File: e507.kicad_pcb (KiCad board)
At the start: 2 copper layers, 1 part

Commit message: work on pcb
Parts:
- added C1: 1µF, Package_DFN_QFN:VQFN-16-1EP_3x3mm_P0.5mm_EP1.6x1.6mm, F.Cu at (178.6, 88.5)
- added C2: 10µF, Package_DFN_QFN:VQFN-16-1EP_3x3mm_P0.5mm_EP1.6x1.6mm, F.Cu at (178.6, 93.8)
- added C3: 1µF, Package_DFN_QFN:VQFN-16-1EP_3x3mm_P0.5mm_EP1.6x1.6mm, F.Cu at (178.6, 99.1)
- added C4: 22µF, Package_DFN_QFN:VQFN-16-1EP_3x3mm_P0.5mm_EP1.6x1.6mm, F.Cu at (178.6, 104.4)
- added C5: 47µF, Package_DFN_QFN:VQFN-16-1EP_3x3mm_P0.5mm_EP1.6x1.6mm, F.Cu at (178.6, 109.8)
- added D1: SMAJ5.0A, Diode_SMD:D_SMA, F.Cu at (187.5, 147.0)
- added J1: GT-USB-7010ASV, usb-port:AMPHENOL_12402012E212A, F.Cu at (196.5, 150.9)
- added J2: DM3CS-SF, microsd:HRS_DM3CS-SF, F.Cu at (192.5, 128.0)
- added J3: SJ-3523-SMT-TR, audio-jack:CUI_SJ-3523-SMT-TR, F.Cu at (197.0, 78.0)
- added J4: SCREEN, Connector:FanPinHeader_1x04_P2.54mm_Vertical, F.Cu at (203.8, 122.7)
- added P1: S2B-PH-SM4-TB, battery-connector:JST_S2B-PH-SM4-TB, F.Cu at (201.2, 139.7)
- added S2: BOOT, flat-button:SW_TS-1088-AR02016, F.Cu at (197.1, 116.5)
- added S3: VOLUME UP, side-button:SW_TL3340AF160QG, F.Cu at (187.0, 74.0)
- added S4: VOLUME DOWN, side-button:SW_TL3340AF160QG, F.Cu at (206.2, 74.0)
- added U1: BQ25185DLHR, charger:IC_BQ25185DLHR, F.Cu at (205.1, 148.7)
- added U2: TPS73633DBVT, ldo:SOT95P280X145-5N, F.Cu at (188.3, 86.5)
- added U3: TPS631000DRLR, buck-boost:SOT50P160X60-8N, F.Cu at (204.3, 132.2)
- added U4: ESP32-S3-WROOM-1U-N16R8, esp32:XCVR_ESP32-S3-WROOM-1U-N16R8, F.Cu at (196.8, 100.6)
- added U5: HS HS91L02W2C01, Display:ER_OLEDM0.91_1x-I2C, F.Cu at (220.2, 93.5)
- added U6: PCM5102APWR, dac:SOP65P640X120-20N, F.Cu at (204.5, 86.0)
- added U7: TPA6132A2RTER, amp:QFN50P300X300X80-16N, F.Cu at (197.0, 88.3)
- added U8: USBLC6-2SC6, Package_TO_SOT_SMD:SOT-23-6, F.Cu at (196.5, 142.5)
- S1: value TS-1088-AR02016 -> RESET
- moved S1 107.8 mm to (189.9, 116.5)
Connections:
- S1 pad 1: unconnected-(S1-Pad1) -> /MCU/IO_EN
- S1 pad 2: unconnected-(S1-Pad2) -> GND

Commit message: fucker
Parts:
- added U5: ER_OLEDM0.91_1x-I2C, Display:ER_OLEDM0.91_1x-I2C, F.Cu at (239.0, 87.3)
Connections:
- J1 pad A6: Net-(J1-D+_A) -> /MCU/USB_D+
- J1 pad A7: Net-(J1-D-_A) -> /MCU/USB_D-
- J1 pad B6: Net-(J1-D+_A) -> /MCU/USB_D+
- J1 pad B7: Net-(J1-D-_A) -> /MCU/USB_D-
- J3 pad 1: unconnected-(J3-SLEEVE-Pad1) -> GNDA
- J3 pad 2: unconnected-(J3-TIP-Pad2) -> Net-(J3-TIP)
- J3 pad 3: unconnected-(J3-RING-Pad3) -> Net-(J3-RING)
- U1 pad 3: /MCU/IO_CHG_STAT2 -> /MCU/IO_CHG_STAT1
- U1 pad 9: /MCU/IO_CHG_STAT1 -> /MCU/IO_CHG_STAT2
- U2 pad 3: /MCU/IO_AUDIO_EN -> /Audio/IO_AMP_EN
- U4 pad 10: /Audio/IO_DAC_BCK -> unconnected-(U4-IO17-Pad10)
- U4 pad 11: /Audio/IO_DAC_LRCK -> unconnected-(U4-IO18-Pad11)
- U4 pad 23: unconnected-(U4-IO21-Pad23) -> /Audio/IO_DAC_SCK
- U4 pad 28: unconnected-(U4-IO35-Pad28) -> /Audio/IO_DAC_DIN
- U4 pad 29: unconnected-(U4-IO36-Pad29) -> /Audio/IO_DAC_BCK
- U4 pad 30: unconnected-(U4-IO37-Pad30) -> /Audio/IO_DAC_LRCK
- U4 pad 8: /MCU/IO_AUDIO_EN -> /Audio/IO_AMP_EN
- U4 pad 9: /Audio/IO_DAC_DIN -> unconnected-(U4-IO16-Pad9)
- U6 pad 12: GND -> /Audio/IO_DAC_SCK
- U6 pad 3: GND -> GNDA
- U6 pad 6: unconnected-(U6-OUTL-Pad6) -> Net-(U6-OUTL)
- U6 pad 7: unconnected-(U6-OUTR-Pad7) -> Net-(U6-OUTR)
- U6 pad 9: GND -> GNDA
- U7 pad 1: unconnected-(U7-INL--Pad1) -> Net-(U7-INL-)
- U7 pad 10: unconnected-(U7-PGND-Pad10) -> GND
- U7 pad 11: unconnected-(U7-CPP-Pad11) -> Net-(U7-CPP)
- U7 pad 12: unconnected-(U7-HPVDD-Pad12) -> Net-(U7-HPVDD)
- U7 pad 13: unconnected-(U7-EN-Pad13) -> /Audio/IO_AMP_EN
- U7 pad 14: unconnected-(U7-VDD-Pad14) -> VSYS
- U7 pad 15: unconnected-(U7-SGND-Pad15) -> GNDA
- U7 pad 16: unconnected-(U7-OUTL-Pad16) -> Net-(J3-TIP)
- U7 pad 17: unconnected-(U7-EP-Pad17) -> GND
- U7 pad 2: unconnected-(U7-INL+-Pad2) -> GND
- U7 pad 3: unconnected-(U7-INR+-Pad3) -> GND
- U7 pad 4: unconnected-(U7-INR--Pad4) -> Net-(U7-INR-)
- U7 pad 5: unconnected-(U7-OUTR-Pad5) -> Net-(J3-RING)
- U7 pad 8: unconnected-(U7-HPVSS-Pad8) -> Net-(U7-HPVSS)
- U7 pad 9: unconnected-(U7-CPN-Pad9) -> Net-(U7-CPN)

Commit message: Finish? schematic
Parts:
- removed the U5 at (239.0, 87.3)
- removed the U5 at (220.2, 93.5)
- removed U8: USBLC6-2SC6, Package_TO_SOT_SMD:SOT-23-6
- added U5: USBLC6-2SC6, Package_TO_SOT_SMD:SOT-23-6, F.Cu at (195.9, 142.9)
- moved J4 11.4 mm to (192.5, 121.5)
- moved J2 5.10 mm to (191.5, 133.0)
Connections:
- D1 pad 1: GND -> VBUS
- D1 pad 2: VBUS -> GND
- J1 pad A6: /MCU/USB_D+ -> Net-(J1-D+_A)
- J1 pad A7: /MCU/USB_D- -> Net-(J1-D-_A)
- J1 pad B6: /MCU/USB_D+ -> Net-(J1-D+_A)
- J1 pad B7: /MCU/USB_D- -> Net-(J1-D-_A)
- U2 pad 2: GND -> GNDA
- U4 pad 10: unconnected-(U4-IO17-Pad10) -> /Audio/IO_DAC_BCK
- U4 pad 11: unconnected-(U4-IO18-Pad11) -> /Audio/IO_DAC_LRCK
- U4 pad 23: /Audio/IO_DAC_SCK -> unconnected-(U4-IO21-Pad23)
- U4 pad 28: /Audio/IO_DAC_DIN -> unconnected-(U4-IO35-Pad28)
- U4 pad 29: /Audio/IO_DAC_BCK -> unconnected-(U4-IO36-Pad29)
- U4 pad 30: /Audio/IO_DAC_LRCK -> unconnected-(U4-IO37-Pad30)
- U4 pad 9: unconnected-(U4-IO16-Pad9) -> /Audio/IO_DAC_DIN
- U6 pad 12: /Audio/IO_DAC_SCK -> GND
- U7 pad 6: unconnected-(U7-G0-Pad6) -> VSYS
- U7 pad 7: unconnected-(U7-G1-Pad7) -> GND

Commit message: holy routing
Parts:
- added C10: 1uF, Capacitor_SMD:C_0201_0603Metric, F.Cu at (71.1, 84.2)
- added C11: 1uF, Capacitor_SMD:C_0201_0603Metric, F.Cu at (71.2, 92.8)
- added C12: 0.1μF, Capacitor_SMD:C_0201_0603Metric, F.Cu at (24.5, 18.5)
- added C13: 10μF, Capacitor_SMD:C_0201_0603Metric, F.Cu at (24.5, 20.2)
- added C14: 2.2μF, Capacitor_SMD:C_0201_0603Metric, F.Cu at (24.5, 22.0)
- added C15: 2.2μF, Capacitor_SMD:C_0201_0603Metric, F.Cu at (24.5, 23.8)
- added C16: 0.1μF, Capacitor_SMD:C_0201_0603Metric, F.Cu at (24.5, 25.5)
- added C17: 10μF, Capacitor_SMD:C_0201_0603Metric, F.Cu at (24.5, 27.2)
- added C18: 0.1μF, Capacitor_SMD:C_0201_0603Metric, F.Cu at (24.5, 29.0)
- added C19: 10μF, Capacitor_SMD:C_0201_0603Metric, F.Cu at (26.9, 18.5)
- added C20: 10μF, Capacitor_SMD:C_0201_0603Metric, F.Cu at (26.9, 20.2)
- added C21: 0.1μF, Capacitor_SMD:C_0201_0603Metric, F.Cu at (26.9, 22.0)
- added C22: 1μF, Capacitor_SMD:C_0201_0603Metric, F.Cu at (26.9, 23.8)
- added C23: 1μF, Capacitor_SMD:C_0201_0603Metric, F.Cu at (26.9, 25.5)
- added C24: 2.2μF, Capacitor_SMD:C_0201_0603Metric, F.Cu at (26.9, 27.2)
- added C25: 2.2μF, Capacitor_SMD:C_0201_0603Metric, F.Cu at (26.9, 29.0)
- added C26: 2.2nF, Capacitor_SMD:C_0201_0603Metric, F.Cu at (29.4, 18.5)
- added C27: 2.2nF, Capacitor_SMD:C_0201_0603Metric, F.Cu at (29.4, 20.2)
- added C28: 1μF, Capacitor_SMD:C_0201_0603Metric, F.Cu at (29.4, 22.0)
- added C29: 1μF, Capacitor_SMD:C_0201_0603Metric, F.Cu at (29.4, 23.8)
- added C6: 10nF, Capacitor_SMD:C_0201_0603Metric, F.Cu at (46.7, 31.0)
- added C7: 1µF, Capacitor_SMD:C_0201_0603Metric, F.Cu at (43.2, 36.5)
- added C8: 1µF, Capacitor_SMD:C_0201_0603Metric, F.Cu at (44.8, 31.0)
- added C9: 100nF, Capacitor_SMD:C_0201_0603Metric, F.Cu at (58.9, 69.8)
- added L1: 1μH, Inductor_SMD:L_0201_0603Metric, F.Cu at (46.0, 86.2)
- added NT1: NetTie_2, NetTie:NetTie-2_SMD_Pad0.5mm, F.Cu at (40.2, 28.8)
- added R1: 18K, Resistor_SMD:R_0201_0603Metric, F.Cu at (54.5, 86.3)
- added R10: 10K?, Resistor_SMD:R_0201_0603Metric, F.Cu at (47.8, 34.8)
- added R11: 570K?, Resistor_SMD:R_0201_0603Metric, F.Cu at (56.9, 69.8)
- added R12: 330K?, Resistor_SMD:R_0201_0603Metric, F.Cu at (57.9, 69.8)
- added R13: 10K, Resistor_SMD:R_0201_0603Metric, F.Cu at (71.0, 83.5)
- added R14: 10K, Resistor_SMD:R_0201_0603Metric, F.Cu at (58.5, 59.9)
- added R15: 10K, Resistor_SMD:R_0201_0603Metric, F.Cu at (72.9, 92.8)
- added R16: 10K, Resistor_SMD:R_0201_0603Metric, F.Cu at (40.1, 42.2)
- added R17: 10K, Resistor_SMD:R_0201_0603Metric, F.Cu at (59.7, 46.8)
- added R18: 10K, Resistor_SMD:R_0201_0603Metric, F.Cu at (49.0, 33.0)
- added R19: 470Ω, Resistor_SMD:R_0201_0603Metric, F.Cu at (29.4, 27.2)
- added R2: 5.1K, Resistor_SMD:R_0201_0603Metric, F.Cu at (53.5, 90.0)
- added R20: 470Ω, Resistor_SMD:R_0201_0603Metric, F.Cu at (29.4, 29.0)
- added R21: 10K, Resistor_SMD:R_0201_0603Metric, F.Cu at (59.7, 61.0)
- added R3: 5.1K, Resistor_SMD:R_0201_0603Metric, F.Cu at (47.5, 89.8)
- added R4: 1K, Resistor_SMD:R_0201_0603Metric, F.Cu at (54.5, 87.0)
- added R5: 10K, Resistor_SMD:R_0201_0603Metric, F.Cu at (54.5, 85.5)
- added R7: 10K, Resistor_SMD:R_0201_0603Metric, F.Cu at (59.7, 58.5)
- added R8: 91K, Resistor_SMD:R_0201_0603Metric, F.Cu at (41.4, 87.0)
- added R9: 511K, Resistor_SMD:R_0201_0603Metric, F.Cu at (42.0, 88.0)
- added RX: RX, TestPoint:TestPoint_Pad_1.5x1.5mm, F.Cu at (44.5, 40.5)
- added TX: TX, TestPoint:TestPoint_Pad_1.5x1.5mm, F.Cu at (42.0, 40.5)
- added U8: SiP32431DR3, Package_TO_SOT_SMD:SOT-363_SC-70-6, F.Cu at (41.3, 64.8)
- C1, C2, C3, C4, C5: footprint Package_DFN_QFN:VQFN-16-1EP_3x3mm_P0.5mm_EP1.6x1.6mm -> Capacitor_SMD:C_0201_0603Metric
- J4: footprint Connector:FanPinHeader_1x04_P2.54mm_Vertical -> Connector_PinHeader_2.54mm:PinHeader_1x04_P2.54mm_Vertical
- moved J4 168.7 mm to (46.3, 37.2), turned to 90 degrees
- moved U3 167.2 mm to (43.5, 86.2), turned to 180 degrees
- moved U7 166.2 mm to (43.2, 25.2)
- moved U1 160.2 mm to (57.5, 86.3), turned to 180 degrees
- moved P1 158.1 mm to (57.9, 73.0), turned to 180 degrees
- moved J2 157.4 mm to (45.5, 74.1)
- moved U4 156.7 mm to (47.6, 52.5), turned to 90 degrees
- moved J1 156.0 mm to (50.1, 96.9)
- moved J3 156.0 mm to (50.6, 24.1)
- moved S3 156.0 mm to (40.6, 20.1)
- moved S4 156.0 mm to (59.8, 20.1)
- moved U6 156.0 mm to (58.1, 32.1)
- moved U5 155.3 mm to (50.6, 88.1)
- moved U2 152.2 mm to (45.5, 33.8), turned to 90 degrees
- moved D1 140.6 mm to (58.8, 90.5), turned to 0 degrees
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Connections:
- J1 pad A6: Net-(J1-D+_A) -> /Power/USB_D+
- J1 pad A7: Net-(J1-D-_A) -> /Power/USB_D-
- J1 pad B6: Net-(J1-D+_A) -> /Power/USB_D+
- J1 pad B7: Net-(J1-D-_A) -> /Power/USB_D-
- J2 pad 4: +3V3_AUDIO -> /MCU/VSD
- J4 pad 1: /MCU/IO_I2C_SDA -> GND
- J4 pad 2: /MCU/IO_I2C_SCL -> +3V3
- J4 pad 3: +3V3 -> /MCU/IO_I2C_SCL
- J4 pad 4: GND -> /MCU/IO_I2C_SDA
- U4 pad 10: /Audio/IO_DAC_BCK -> /MCU/IO_SD_DAT1
- U4 pad 12: /MCU/IO_SD_DAT2 -> unconnected-(U4-IO8-Pad12)
- U4 pad 13: /MCU/USB_D- -> /Power/USB_D-
- U4 pad 14: /MCU/USB_D+ -> /Power/USB_D+
- U4 pad 17: /MCU/IO_SD_DAT3 -> /MCU/IO_CHG_STAT2
- U4 pad 18: /MCU/IO_VOLUME_UP -> /MCU/IO_CHG_STAT1
- U4 pad 19: /MCU/IO_VOLUME_DOWN -> /MCU/IO_BAT_V
- U4 pad 20: /MCU/IO_BAT_V -> /Audio/IO_AMP_EN
- U4 pad 21: /MCU/IO_CHG_STAT1 -> /Audio/IO_DAC_DIN
- U4 pad 22: /MCU/IO_CHG_STAT2 -> /Audio/IO_DAC_BCK
- U4 pad 25: unconnected-(U4-IO48-Pad25) -> /MCU/IO_VOLUME_DOWN
- U4 pad 34: unconnected-(U4-IO41-Pad34) -> /MCU/IO_I2C_SDA
- U4 pad 35: unconnected-(U4-IO42-Pad35) -> /MCU/IO_I2C_SCL
- U4 pad 36: unconnected-(U4-RXD0-Pad36) -> Net-(U4-RXD0)
- U4 pad 37: unconnected-(U4-TXD0-Pad37) -> Net-(U4-TXD0)
- U4 pad 38: /MCU/IO_I2C_SCL -> unconnected-(U4-IO2-Pad38)
- U4 pad 39: /MCU/IO_I2C_SDA -> /MCU/IO_VOLUME_UP
- U4 pad 4: /MCU/IO_SD_CMD -> /MCU/IO_SD_EN
- U4 pad 5: /MCU/IO_SD_CLK -> /MCU/IO_SD_DAT2
- U4 pad 6: /MCU/IO_SD_DAT0 -> /MCU/IO_SD_DAT3
- U4 pad 7: /MCU/IO_SD_DAT1 -> /MCU/IO_SD_CMD
- U4 pad 8: /Audio/IO_AMP_EN -> /MCU/IO_SD_CLK
- U4 pad 9: /Audio/IO_DAC_DIN -> /MCU/IO_SD_DAT0
- U5 pad 1: Net-(J1-D+_A) -> /Power/USB_D-
- U5 pad 3: Net-(J1-D-_A) -> /Power/USB_D+
- U5 pad 4: /MCU/USB_D- -> /Power/USB_D+
- U5 pad 6: /MCU/USB_D+ -> /Power/USB_D-
- U7 pad 10: GND -> GNDA
- U7 pad 14: VSYS -> +3V3_AUDIO
- U7 pad 17: GND -> GNDA
- U7 pad 2: GND -> GNDA
- U7 pad 3: GND -> GNDA
- U7 pad 6: VSYS -> +3V3_AUDIO
- U7 pad 7: GND -> GNDA
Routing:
- net +3V3: track 0.00 -> 125.4 mm, vias 0 -> 5
- net VSYS: track 0.00 -> 61.0 mm, vias 0 -> 3
- net /MCU/IO_CHG_STAT2: track 0.00 -> 37.9 mm
- net /MCU/IO_CHG_STAT1: track 0.00 -> 36.9 mm
- net /MCU/IO_VOLUME_DOWN: track 0.00 -> 28.8 mm
- net /MCU/IO_VOLUME_UP: track 0.00 -> 22.9 mm
- net /MCU/IO_BAT_V: track 0.00 -> 20.1 mm
- net /Power/VBAT: track 0.00 -> 18.9 mm
- net /MCU/IO_I2C_SDA: track 0.00 -> 10.4 mm
- net GND: track 0.00 -> 10.3 mm, vias 0 -> 5
- net /MCU/VSD: track 0.00 -> 9.98 mm
- net VBUS: track 0.00 -> 9.27 mm, vias 0 -> 4
- net /MCU/IO_I2C_SCL: track 0.00 -> 8.96 mm
- net /MCU/IO_SD_DAT3: track 0.00 -> 7.52 mm
- net /MCU/IO_SD_DAT2: track 0.00 -> 7.47 mm
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- added copper zone on F.Cu, net GND
- added copper zone on In1.Cu, net GND
- added copper zone on F.Cu, net GNDA
- added copper zone on In2.Cu, net VBUS
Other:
- board outline added: 25 x 80 mm
- copper layers 2 -> 4

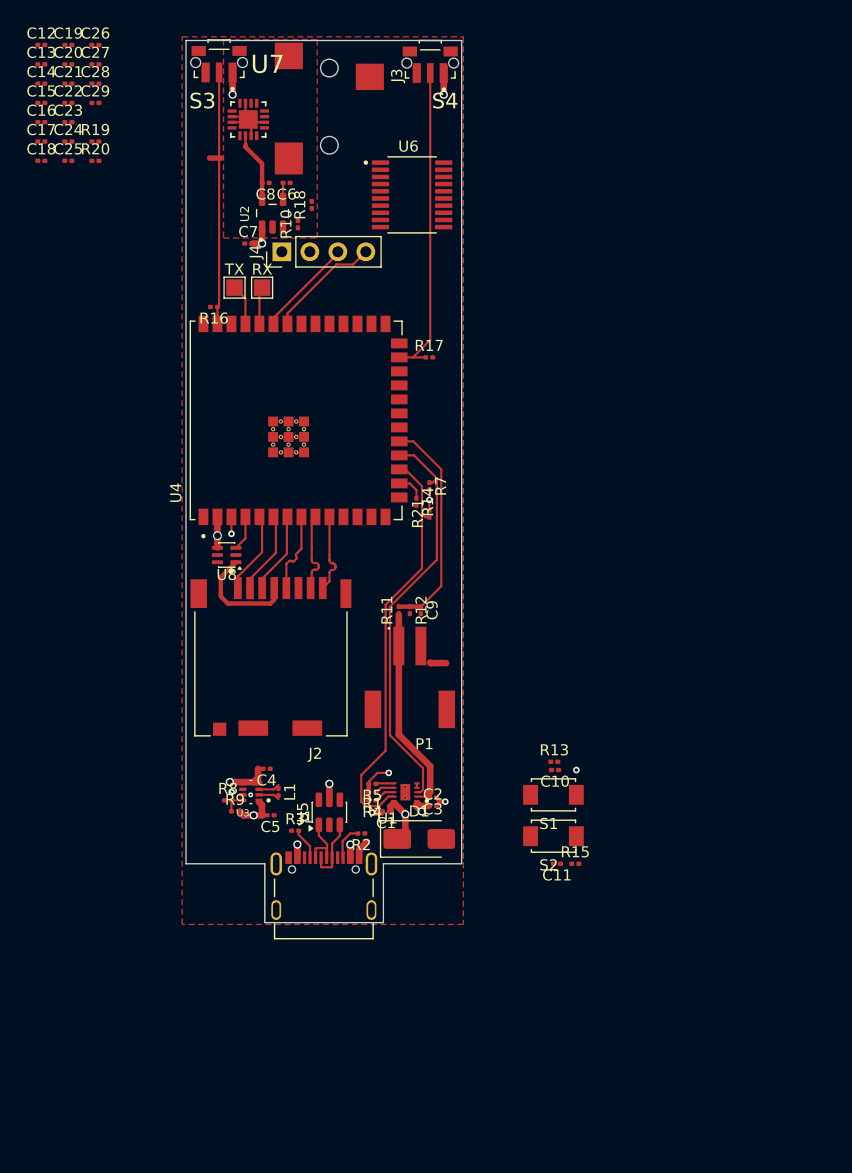
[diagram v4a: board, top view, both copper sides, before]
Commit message: shrink canvas
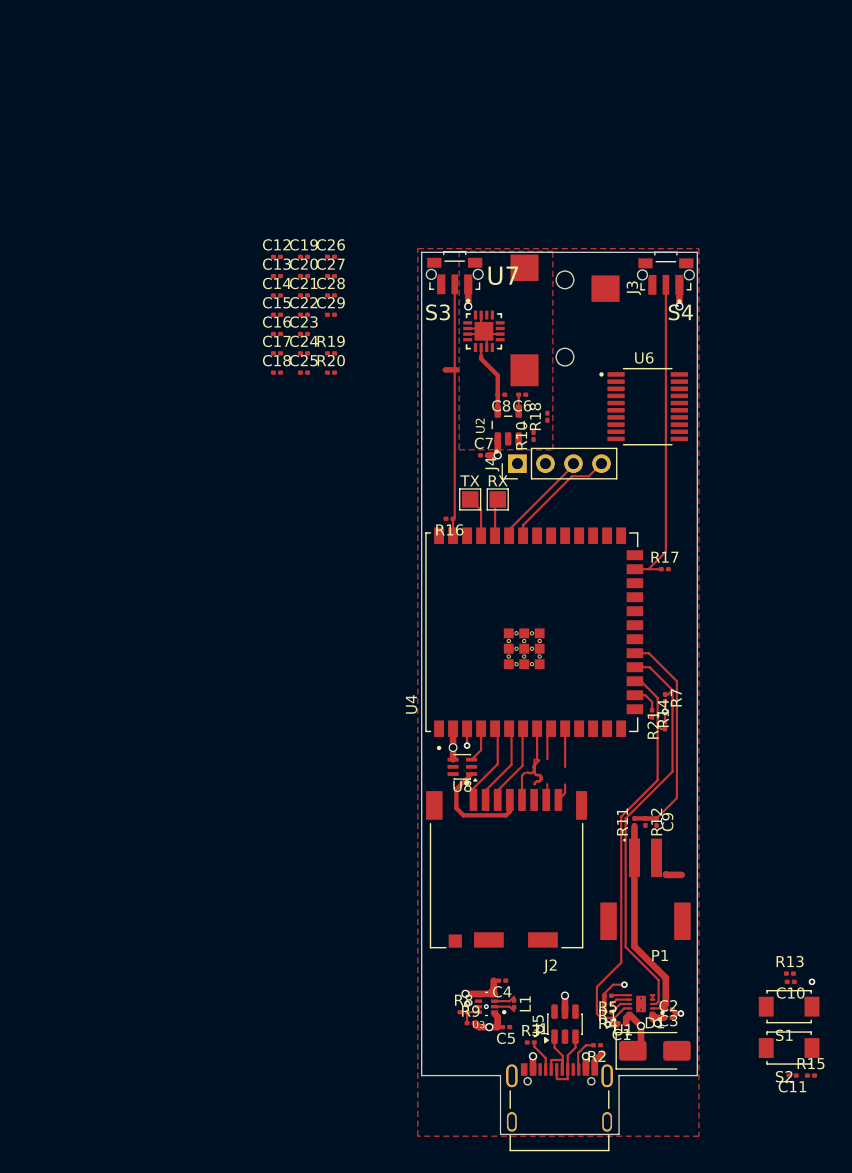
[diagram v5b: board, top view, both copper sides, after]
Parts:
- moved J2 28.7 mm to (66.9, 93.3)
- moved C10 28.7 mm to (92.4, 103.5)
- moved C11 28.7 mm to (92.6, 112.0)
- moved C12 28.7 mm to (45.9, 37.7)
- moved C13 28.7 mm to (45.9, 39.5)
- moved C14 28.7 mm to (45.9, 41.2)
- moved C15 28.7 mm to (45.9, 43.0)
- moved C16 28.7 mm to (45.9, 44.7)
- moved C17 28.7 mm to (45.9, 46.5)
- moved C18 28.7 mm to (45.9, 48.2)
- moved C19 28.7 mm to (48.3, 37.7)
- moved C20 28.7 mm to (48.3, 39.5)
- moved C21 28.7 mm to (48.3, 41.2)
- moved C22 28.7 mm to (48.3, 43.0)
- moved C23 28.7 mm to (48.3, 44.7)
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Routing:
- net /MCU/IO_SD_CLK: track 7.37 -> 12.7 mm
- net /MCU/IO_SD_DAT0: track 7.47 -> 4.38 mm
- net /MCU/IO_SD_DAT1: track 7.36 -> 5.13 mm
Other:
- outline, holes or cut-outs redrawn

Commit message: some placements
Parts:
- moved C20 33.0 mm to (80.2, 48.0)
- moved C21 32.8 mm to (80.2, 49.0)
- moved C15 26.3 mm to (71.5, 48.8), turned to 90 degrees
- moved R17 6.36 mm to (80.7, 72.4)
- moved U6 4.89 mm to (74.6, 50.6)
- moved J3 4.60 mm to (72.0, 38.7)
- moved R18 1.34 mm to (70.0, 53.5)
- renumbered RX to TP1, TX to TP2
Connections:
- U4 pad 11: /Audio/IO_DAC_LRCK -> unconnected-(U4-IO18-Pad11)
- U4 pad 20: /Audio/IO_AMP_EN -> /MCU/IO_VOLUME_DOWN
- U4 pad 21: /Audio/IO_DAC_DIN -> /Audio/IO_AMP_EN
- U4 pad 22: /Audio/IO_DAC_BCK -> unconnected-(U4-IO14-Pad22)
- U4 pad 23: unconnected-(U4-IO21-Pad23) -> /Audio/IO_DAC_LRCK
- U4 pad 24: unconnected-(U4-IO47-Pad24) -> /Audio/IO_DAC_DIN
- U4 pad 25: /MCU/IO_VOLUME_DOWN -> /Audio/IO_DAC_BCK
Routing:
- net /Audio/IO_DAC_LRCK: track 0.00 -> 20.5 mm
- net /Audio/IO_DAC_DIN: track 0.00 -> 18.5 mm
- net /Audio/IO_DAC_BCK: track 0.00 -> 15.8 mm
- net /MCU/IO_VOLUME_DOWN: track 28.8 -> 35.2 mm
- net /MCU/IO_SD_CLK: track 12.7 -> 7.37 mm
- net /MCU/IO_SD_DAT0: track 4.38 -> 7.47 mm
- net /MCU/IO_SD_DAT1: track 5.13 -> 7.36 mm
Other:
- board size 25 x 80 mm -> 25 x 84.8 mm

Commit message: fix sd card pullups
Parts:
- removed TP1: RX, TestPoint:TestPoint_Pad_1.5x1.5mm
- removed TP2: TX, TestPoint:TestPoint_Pad_1.5x1.5mm
- added C30: 1µF, Capacitor_SMD:C_0201_0603Metric, F.Cu at (55.7, 82.9)
- added C31: 0.1µF, Capacitor_SMD:C_0201_0603Metric, F.Cu at (55.7, 84.6)
- added R23: 10K, Resistor_SMD:R_0201_0603Metric, F.Cu at (55.7, 86.4)
- added R24: 10K, Resistor_SMD:R_0201_0603Metric, F.Cu at (55.7, 88.1)
- added R25: 10K, Resistor_SMD:R_0201_0603Metric, F.Cu at (55.7, 89.9)
- added R26: 10K, Resistor_SMD:R_0201_0603Metric, F.Cu at (55.7, 91.6)
- added R27: 10K, Resistor_SMD:R_0201_0603Metric, F.Cu at (55.7, 93.4)
- C10, C11: value 1uF -> 1µF
- moved C20 0.82 mm to (81.0, 48.0), turned to -90 degrees
- moved C21 0.53 mm to (80.0, 48.5), turned to 90 degrees
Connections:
- net /MCU/VSD renamed VSD
- R21 pad 1: /MCU/IO_CHG_STAT2 -> /MCU/IO_CHG_STAT1
- R7 pad 1: /MCU/IO_CHG_STAT1 -> /MCU/IO_CHG_STAT2
- U1 pad 3: /MCU/IO_CHG_STAT1 -> /MCU/IO_CHG_STAT2
- U1 pad 9: /MCU/IO_CHG_STAT2 -> /MCU/IO_CHG_STAT1
- U4 pad 36: Net-(U4-RXD0) -> unconnected-(U4-RXD0-Pad36)
- U4 pad 37: Net-(U4-TXD0) -> unconnected-(U4-TXD0-Pad37)
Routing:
- net Net-(U4-RXD0): track 4.08 -> 0.00 mm
- net Net-(U4-TXD0): track 3.70 -> 0.00 mm
- net Net-(U6-LDOO): track 0.00 -> 2.55 mm
- net GND: track 10.3 -> 11.4 mm

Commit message: switch to stm32, wire audio section
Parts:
- removed U4: ESP32-S3-WROOM-1U-N16R8, esp32:XCVR_ESP32-S3-WROOM-1U-N16R8
- added C32: 100nF, Capacitor_SMD:C_0402_1005Metric, F.Cu at (69.8, 65.8)
- added C33: 100nF, Capacitor_SMD:C_0402_1005Metric, F.Cu at (66.4, 65.3)
- added C34: 100nF, Capacitor_SMD:C_0402_1005Metric, F.Cu at (62.0, 69.3)
- added C35: 100nF, Capacitor_SMD:C_0402_1005Metric, F.Cu at (61.2, 76.5)
- added C36: 100nF, Capacitor_SMD:C_0402_1005Metric, F.Cu at (67.0, 82.0)
- added C37: 4.7µF, Capacitor_SMD:C_0402_1005Metric, F.Cu at (78.0, 75.2)
- added R22: 10K, Resistor_SMD:R_0402_1005Metric, F.Cu at (64.5, 80.5)
- added U9: STM32F446RETx, Package_QFP:LQFP-64_10x10mm_P0.5mm, F.Cu at (68.7, 73.5)
- C1, C10, C12, C13, C14, C15, C16, C17, C18, C19, C2, C20, C21, C22, C23, C24, C25, C26, C27, C28, C29, C3, C30, C31, C4, C5, C6, C7, C8, C9: footprint Capacitor_SMD:C_0201_0603Metric -> Capacitor_SMD:C_0402_1005Metric
- C11: value 1µF -> 100nF; footprint Capacitor_SMD:C_0201_0603Metric -> Capacitor_SMD:C_0402_1005Metric
- L1: footprint Inductor_SMD:L_0201_0603Metric -> Inductor_SMD:L_1008_2520Metric
- R1, R10, R11, R12, R13, R14, R15, R16, R17, R18, R19, R2, R20, R21, R23, R24, R25, R26, R27, R3, R4, R5, R7, R8, R9: footprint Resistor_SMD:R_0201_0603Metric -> Resistor_SMD:R_0402_1005Metric
- moved S1 51.3 mm to (63.5, 63.2), turned to 90 degrees
- moved R15 50.5 mm to (72.8, 66.2), turned to -90 degrees
- moved C10 49.1 mm to (61.0, 65.7), turned to -90 degrees
- moved R13 46.0 mm to (63.0, 67.2)
- moved S2 45.5 mm to (76.5, 66.8)
- moved C11 39.4 mm to (76.5, 76.0), turned to -135 degrees
- moved C19 33.2 mm to (73.8, 59.0), turned to 180 degrees
- moved C12 32.4 mm to (75.5, 50.8), turned to 180 degrees
- moved C24 32.4 mm to (80.7, 46.5), turned to 180 degrees
- moved C22 32.3 mm to (80.2, 47.9), turned to 90 degrees
- moved C13 31.4 mm to (75.5, 49.8)
- moved C23 31.2 mm to (79.2, 49.4), turned to 90 degrees
- moved C18 30.4 mm to (74.8, 57.5), turned to 180 degrees
- moved C25 30.0 mm to (78.1, 44.5), turned to 180 degrees
- moved C14 27.0 mm to (72.0, 48.1), turned to 90 degrees
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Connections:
- net /MCU/IO_EN renamed /MCU/IO_RESET
- net /MCU/IO_SD_DAT1 renamed Net-(J2-DAT1)
- net /MCU/IO_SD_DAT2 renamed Net-(J2-DAT2)
- net /MCU/IO_SD_DAT3 renamed Net-(J2-CD/DAT3)
- C11 pad 1: /MCU/IO_BOOT -> +3V3
- C28 pad 1: /Audio/DAC_L -> /Audio/DAC_R
- C29 pad 1: /Audio/DAC_R -> /Audio/DAC_L
- R10 pad 1: /Audio/IO_AMP_EN -> /MCU/IO_AUDIO_EN
- R15 pad 1: +3V3 -> GND
- S2 pad 1: /MCU/IO_BOOT -> +3V3
- S2 pad 2: GND -> /MCU/IO_BOOT
- U2 pad 2: GNDA -> GND
- U2 pad 3: /Audio/IO_AMP_EN -> /MCU/IO_AUDIO_EN
- U6 pad 10: GND -> GNDA
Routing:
- net +3V3: track 125.4 -> 172.2 mm, vias 5 -> 7
- net +3V3_AUDIO: track 6.39 -> 50.9 mm, vias 0 -> 3
- net GNDA: track 7.17 -> 45.5 mm, vias 0 -> 19
- net /Power/USB_D+: track 5.94 -> 38.9 mm
- net /Power/USB_D-: track 6.01 -> 38.6 mm
- net VSYS: track 61.0 -> 87.1 mm
- net GND: track 11.4 -> 34.1 mm, vias 5 -> 40
- net VSD: track 9.98 -> 27.5 mm
- net /MCU/IO_SD_CMD: track 7.41 -> 21.2 mm
- net Net-(J3-RING): track 0.00 -> 11.9 mm, vias 0 -> 2
- net /MCU/IO_SD_CLK: track 7.37 -> 18.6 mm
- net /MCU/IO_I2C_SDA: track 10.4 -> 0.00 mm
- net Net-(J3-TIP): track 0.00 -> 9.43 mm
- net /MCU/IO_I2C_SCL: track 8.96 -> 0.00 mm
- net /Audio/IO_DAC_BCK: track 15.8 -> 24.1 mm, vias 0 -> 2
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- added copper zone on In1.Cu, net GNDA
- removed copper zone on F.Cu, net GNDA
